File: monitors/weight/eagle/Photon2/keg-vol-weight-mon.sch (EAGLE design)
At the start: 18 parts, among them U1 PHOTON2

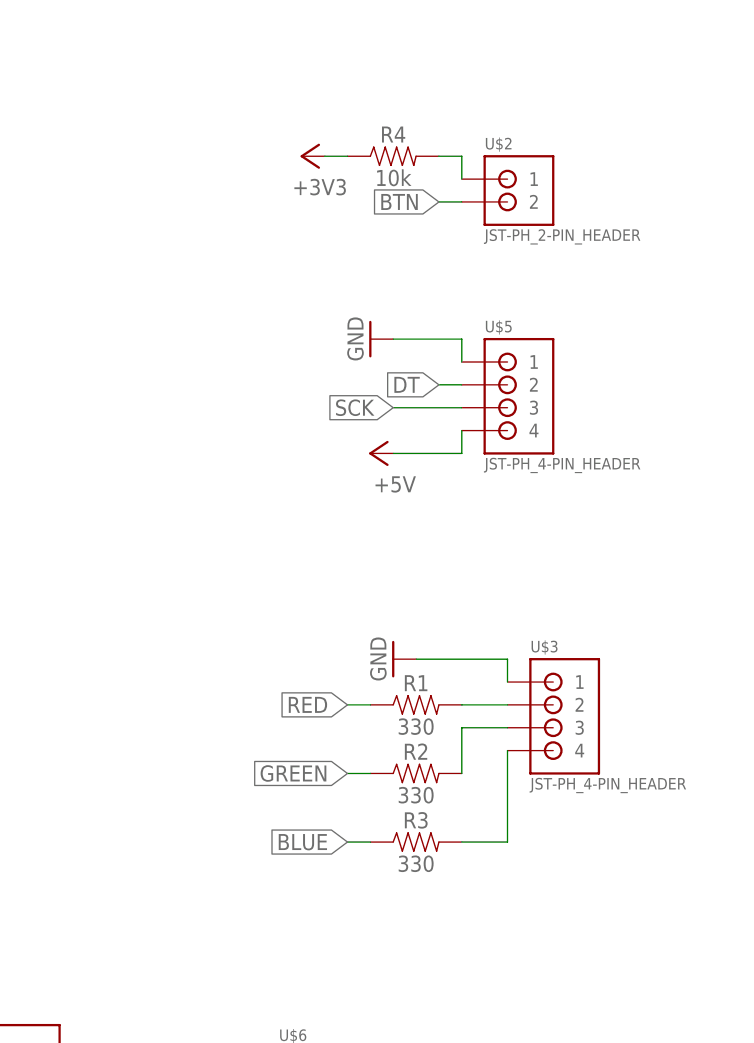
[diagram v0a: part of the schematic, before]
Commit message: Got the device registration process working
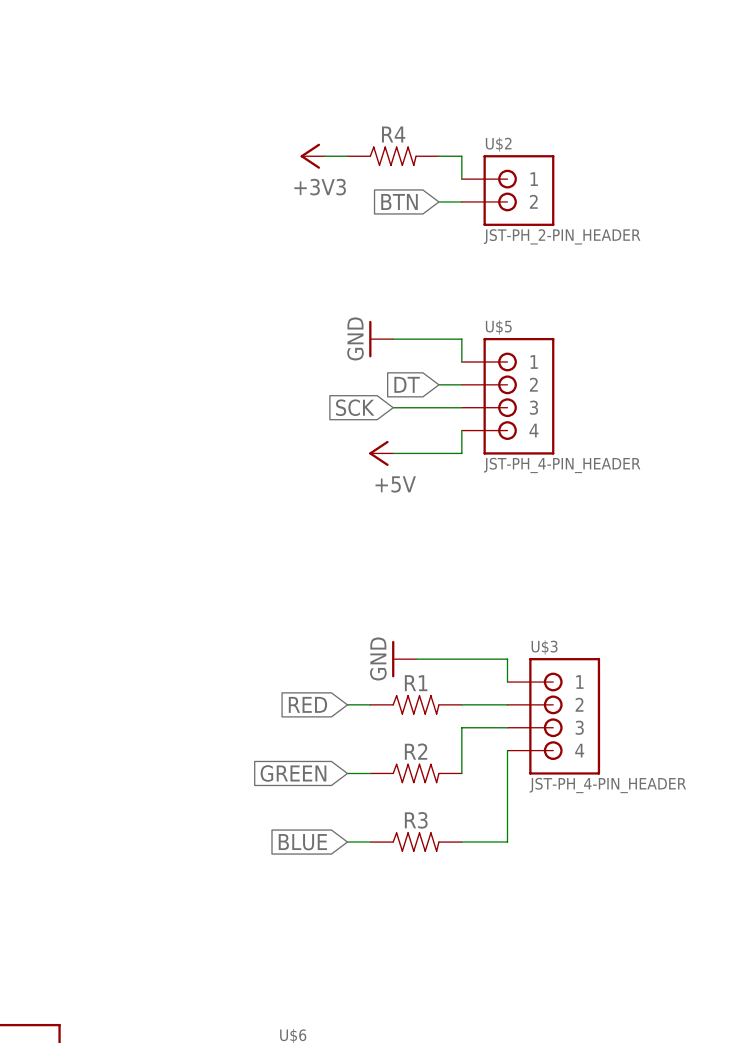
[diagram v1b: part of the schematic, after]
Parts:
- R1, R2, R3: value 330 -> (none)
- R4: value 10k -> (none)
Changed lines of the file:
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@@
 </classes>
 <parts>
-<part name="R1" library="SparkFun-Resistors" library_urn="urn:adsk.eagle:library:532" deviceset="RESISTOR" device="AXIAL-0.3" package3d_urn="urn:adsk.eagle:package:39658/2" value="330"/>
-<part name="R2" library="SparkFun-Resistors" library_urn="urn:adsk.eagle:library:532" deviceset="RESISTOR" device="AXIAL-0.3" package3d_urn="urn:adsk.eagle:package:39658/2" value="330"/>
-<part name="R3" library="SparkFun-Resistors" library_urn="urn:adsk.eagle:library:532" deviceset="RESISTOR" device="AXIAL-0.3" package3d_urn="urn:adsk.eagle:package:39658/2" value="330"/>
+<part name="R1" library="SparkFun-Resistors" library_urn="urn:adsk.eagle:library:532" deviceset="RESISTOR" device="AXIAL-0.3" package3d_urn="urn:adsk.eagle:package:39658/2" value=" "/>
+<part name="R2" library="SparkFun-Resistors" library_urn="urn:adsk.eagle:library:532" deviceset="RESISTOR" device="AXIAL-0.3" package3d_urn="urn:adsk.eagle:package:39658/2" value=" "/>
+<part name="R3" library="SparkFun-Resistors" library_urn="urn:adsk.eagle:library:532" deviceset="RESISTOR" device="AXIAL-0.3" package3d_urn="urn:adsk.eagle:package:39658/2" value=" "/>
 <part name="U$3" library="SRG" deviceset="JST-PH_4-PIN_HEADER" device=""/>
 <part name="U$5" library="SRG" deviceset="JST-PH_4-PIN_HEADER" device=""/>
@@
 <part name="GND6" library="supply1" library_urn="urn:adsk.eagle:library:371" deviceset="GND" device=""/>
 <part name="U$2" library="SRG" deviceset="JST-PH_2-PIN_HEADER" device=""/>
-<part name="R4" library="SparkFun-Resistors" library_urn="urn:adsk.eagle:library:532" deviceset="RESISTOR" device="AXIAL-0.3" package3d_urn="urn:adsk.eagle:package:39658/2" value="10k"/>
+<part name="R4" library="SparkFun-Resistors" library_urn="urn:adsk.eagle:library:532" deviceset="RESISTOR" device="AXIAL-0.3" package3d_urn="urn:adsk.eagle:package:39658/2" value=" "/>
 <part name="+3V2" library="supply1" library_urn="urn:adsk.eagle:library:371" deviceset="+3V3" device=""/>
 <part name="P+2" library="supply1" library_urn="urn:adsk.eagle:library:371" deviceset="+5V" device=""/>
